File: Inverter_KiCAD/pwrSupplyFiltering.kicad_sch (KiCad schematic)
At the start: 10 parts

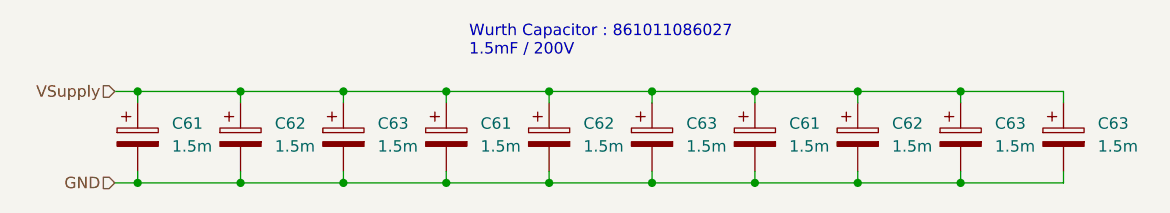
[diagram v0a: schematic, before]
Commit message: clear schematic errors
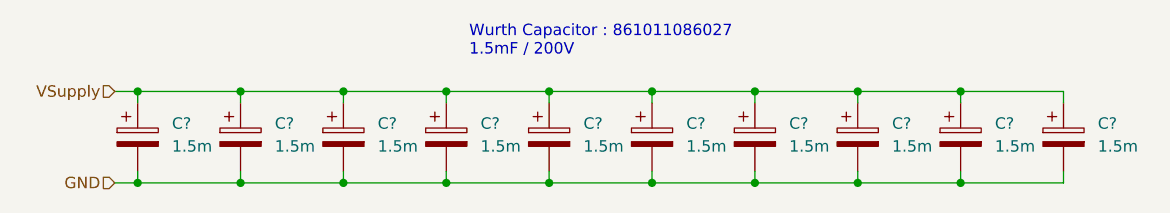
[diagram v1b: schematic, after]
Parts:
- renumbered C63 to C?, C61 to C?, C62 to C?
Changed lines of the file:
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@@
   (symbol (lib_id "Device:C_Polarized") (at 90.17 63.5 0) (unit 1)
     (in_bom yes) (on_board yes) (dnp no) (fields_autoplaced)
-    (property "Reference" "C63" (at 93.98 61.976 0)
+    (property "Reference" "C?" (at 93.98 61.976 0)
       (effects (font (size 1.27 1.27)) (justify left))
     )
@@
       (project "Inverter_KiCAD"
         (path "/5e6c1e3f-0815-454a-8acb-8e3e2d064875"
-          (reference "C63") (unit 1)
-        )
-        (path "/5e6c1e3f-0815-454a-8acb-8e3e2d064875/3abd505c-2b96-4cc2-9359-42e0642ca937"
-          (reference "C65") (unit 1)
+          (reference "C?") (unit 1)
+        )
+        (path "/5e6c1e3f-0815-454a-8acb-8e3e2d064875/3abd505c-2b96-4cc2-9359-42e0642ca937"
+          (reference "C1003") (unit 1)
         )
       )
@@
   (symbol (lib_id "Device:C_Polarized") (at 135.89 63.5 0) (unit 1)
     (in_bom yes) (on_board yes) (dnp no)
-    (property "Reference" "C61" (at 139.7 61.976 0)
+    (property "Reference" "C?" (at 139.7 61.976 0)
       (effects (font (size 1.27 1.27)) (justify left))
     )
@@
       (project "Inverter_KiCAD"
         (path "/5e6c1e3f-0815-454a-8acb-8e3e2d064875"
-          (reference "C61") (unit 1)
-        )
-        (path "/5e6c1e3f-0815-454a-8acb-8e3e2d064875/3abd505c-2b96-4cc2-9359-42e0642ca937"
-          (reference "C67") (unit 1)
+          (reference "C?") (unit 1)
+        )
+        (path "/5e6c1e3f-0815-454a-8acb-8e3e2d064875/3abd505c-2b96-4cc2-9359-42e0642ca937"
+          (reference "C1007") (unit 1)
         )
       )
@@
   (symbol (lib_id "Device:C_Polarized") (at 170.18 63.5 0) (unit 1)
     (in_bom yes) (on_board yes) (dnp no) (fields_autoplaced)
-    (property "Reference" "C63" (at 173.99 61.976 0)
+    (property "Reference" "C?" (at 173.99 61.976 0)
       (effects (font (size 1.27 1.27)) (justify left))
     )
@@
       (project "Inverter_KiCAD"
         (path "/5e6c1e3f-0815-454a-8acb-8e3e2d064875"
-          (reference "C63") (unit 1)
-        )
-        (path "/5e6c1e3f-0815-454a-8acb-8e3e2d064875/3abd505c-2b96-4cc2-9359-42e0642ca937"
-          (reference "C70") (unit 1)
+          (reference "C?") (unit 1)
+        )
+        (path "/5e6c1e3f-0815-454a-8acb-8e3e2d064875/3abd505c-2b96-4cc2-9359-42e0642ca937"
+          (reference "C1010") (unit 1)
         )
       )
@@
   (symbol (lib_id "Device:C_Polarized") (at 67.31 63.5 0) (unit 1)
     (in_bom yes) (on_board yes) (dnp no)
-    (property "Reference" "C61" (at 71.12 61.976 0)
+    (property "Reference" "C?" (at 71.12 61.976 0)
       (effects (font (size 1.27 1.27)) (justify left))
     )
@@
       (project "Inverter_KiCAD"
         (path "/5e6c1e3f-0815-454a-8acb-8e3e2d064875"
-          (reference "C61") (unit 1)
-        )
-        (path "/5e6c1e3f-0815-454a-8acb-8e3e2d064875/3abd505c-2b96-4cc2-9359-42e0642ca937"
-          (reference "C61") (unit 1)
+          (reference "C?") (unit 1)
+        )
+        (path "/5e6c1e3f-0815-454a-8acb-8e3e2d064875/3abd505c-2b96-4cc2-9359-42e0642ca937"
+          (reference "C1001") (unit 1)
         )
       )
@@
   (symbol (lib_id "Device:C_Polarized") (at 78.74 63.5 0) (unit 1)
     (in_bom yes) (on_board yes) (dnp no) (fields_autoplaced)
-    (property "Reference" "C62" (at 82.55 61.976 0)
+    (property "Reference" "C?" (at 82.55 61.976 0)
       (effects (font (size 1.27 1.27)) (justify left))
     )
@@
       (project "Inverter_KiCAD"
         (path "/5e6c1e3f-0815-454a-8acb-8e3e2d064875"
-          (reference "C62") (unit 1)
-        )
-        (path "/5e6c1e3f-0815-454a-8acb-8e3e2d064875/3abd505c-2b96-4cc2-9359-42e0642ca937"
-          (reference "C63") (unit 1)
+          (reference "C?") (unit 1)
+        )
+        (path "/5e6c1e3f-0815-454a-8acb-8e3e2d064875/3abd505c-2b96-4cc2-9359-42e0642ca937"
+          (reference "C1002") (unit 1)
         )
       )
@@
   (symbol (lib_id "Device:C_Polarized") (at 101.6 63.5 0) (unit 1)
     (in_bom yes) (on_board yes) (dnp no)
-    (property "Reference" "C61" (at 105.41 61.976 0)
+    (property "Reference" "C?" (at 105.41 61.976 0)
       (effects (font (size 1.27 1.27)) (justify left))
     )
@@
       (project "Inverter_KiCAD"
         (path "/5e6c1e3f-0815-454a-8acb-8e3e2d064875"
-          (reference "C61") (unit 1)
-        )
-        (path "/5e6c1e3f-0815-454a-8acb-8e3e2d064875/3abd505c-2b96-4cc2-9359-42e0642ca937"
-          (reference "C62") (unit 1)
+          (reference "C?") (unit 1)
+        )
+        (path "/5e6c1e3f-0815-454a-8acb-8e3e2d064875/3abd505c-2b96-4cc2-9359-42e0642ca937"
+          (reference "C1004") (unit 1)
         )
       )
@@
   (symbol (lib_id "Device:C_Polarized") (at 147.32 63.5 0) (unit 1)
     (in_bom yes) (on_board yes) (dnp no) (fields_autoplaced)
-    (property "Reference" "C62" (at 151.13 61.976 0)
+    (property "Reference" "C?" (at 151.13 61.976 0)
       (effects (font (size 1.27 1.27)) (justify left))
     )
@@
       (project "Inverter_KiCAD"
         (path "/5e6c1e3f-0815-454a-8acb-8e3e2d064875"
-          (reference "C62") (unit 1)
-        )
-        (path "/5e6c1e3f-0815-454a-8acb-8e3e2d064875/3abd505c-2b96-4cc2-9359-42e0642ca937"
-          (reference "C68") (unit 1)
+          (reference "C?") (unit 1)
+        )
+        (path "/5e6c1e3f-0815-454a-8acb-8e3e2d064875/3abd505c-2b96-4cc2-9359-42e0642ca937"
+          (reference "C1008") (unit 1)
         )
       )
@@
   (symbol (lib_id "Device:C_Polarized") (at 158.75 63.5 0) (unit 1)
     (in_bom yes) (on_board yes) (dnp no) (fields_autoplaced)
-    (property "Reference" "C63" (at 162.56 61.976 0)
+    (property "Reference" "C?" (at 162.56 61.976 0)
       (effects (font (size 1.27 1.27)) (justify left))
     )
@@
       (project "Inverter_KiCAD"
         (path "/5e6c1e3f-0815-454a-8acb-8e3e2d064875"
-          (reference "C63") (unit 1)
-        )
-        (path "/5e6c1e3f-0815-454a-8acb-8e3e2d064875/3abd505c-2b96-4cc2-9359-42e0642ca937"
-          (reference "C69") (unit 1)
+          (reference "C?") (unit 1)
+        )
+        (path "/5e6c1e3f-0815-454a-8acb-8e3e2d064875/3abd505c-2b96-4cc2-9359-42e0642ca937"
+          (reference "C1009") (unit 1)
         )
       )
@@
   (symbol (lib_id "Device:C_Polarized") (at 124.46 63.5 0) (unit 1)
     (in_bom yes) (on_board yes) (dnp no) (fields_autoplaced)
-    (property "Reference" "C63" (at 128.27 61.976 0)
+    (property "Reference" "C?" (at 128.27 61.976 0)
       (effects (font (size 1.27 1.27)) (justify left))
     )
@@
       (project "Inverter_KiCAD"
         (path "/5e6c1e3f-0815-454a-8acb-8e3e2d064875"
-          (reference "C63") (unit 1)
-        )
-        (path "/5e6c1e3f-0815-454a-8acb-8e3e2d064875/3abd505c-2b96-4cc2-9359-42e0642ca937"
-          (reference "C66") (unit 1)
+          (reference "C?") (unit 1)
+        )
+        (path "/5e6c1e3f-0815-454a-8acb-8e3e2d064875/3abd505c-2b96-4cc2-9359-42e0642ca937"
+          (reference "C1006") (unit 1)
         )
       )
@@
   (symbol (lib_id "Device:C_Polarized") (at 113.03 63.5 0) (unit 1)
     (in_bom yes) (on_board yes) (dnp no) (fields_autoplaced)
-    (property "Reference" "C62" (at 116.84 61.976 0)
+    (property "Reference" "C?" (at 116.84 61.976 0)
       (effects (font (size 1.27 1.27)) (justify left))
     )
@@
       (project "Inverter_KiCAD"
         (path "/5e6c1e3f-0815-454a-8acb-8e3e2d064875"
-          (reference "C62") (unit 1)
-        )
-        (path "/5e6c1e3f-0815-454a-8acb-8e3e2d064875/3abd505c-2b96-4cc2-9359-42e0642ca937"
-          (reference "C64") (unit 1)
-        )
-      )
+          (reference "C?") (unit 1)
+        )
+        (path "/5e6c1e3f-0815-454a-8acb-8e3e2d064875/3abd505c-2b96-4cc2-9359-42e0642ca937"
+          (reference "C1005") (unit 1)
+        )
+      )

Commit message: end of sch, start pcb
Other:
- company: (none) -> ENSEA
- title: (none) -> AAP Inverter
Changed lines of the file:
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@@
 (kicad_sch (version 20230121) (generator eeschema)
   (paper "A4")
+  (title_block
+    (title "AAP Inverter")
+    (date "2023-05-01")
+    (company "ENSEA")
+  )
   (junction (at 90.17 58.42) (diameter 0) (color 0 0 0 0)
   )

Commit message: rooting done
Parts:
- removed C?: 1.5m, Capacitor_THT:CP_Radial_D35.0mm_P10.00mm_SnapIn, symbol Device:C_Polarized

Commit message: change pcb
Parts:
- removed C? (x4): 1.5m, Capacitor_THT:CP_Radial_D35.0mm_P10.00mm_SnapIn, symbol Device:C_Polarized
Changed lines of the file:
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@@
     (company "ENSEA")
   )
-  (junction (at 90.17 58.42) (diameter 0) (color 0 0 0 0)
-  )
-  (junction (at 113.03 58.42) (diameter 0) (color 0 0 0 0)
-  )
   (junction (at 147.32 68.58) (diameter 0) (color 0 0 0 0)
   )
-  (junction (at 78.74 68.58) (diameter 0) (color 0 0 0 0)
-  )
-  (junction (at 101.6 58.42) (diameter 0) (color 0 0 0 0)
-  )
   (junction (at 124.46 58.42) (diameter 0) (color 0 0 0 0)
   )
@@
   (junction (at 147.32 58.42) (diameter 0) (color 0 0 0 0)
   )
-  (junction (at 113.03 68.58) (diameter 0) (color 0 0 0 0)
-  )
-  (junction (at 90.17 68.58) (diameter 0) (color 0 0 0 0)
-  )
-  (junction (at 101.6 68.58) (diameter 0) (color 0 0 0 0)
-  )
-  (junction (at 78.74 58.42) (diameter 0) (color 0 0 0 0)
-  )
   (junction (at 124.46 68.58) (diameter 0) (color 0 0 0 0)
   )
@@
     (stroke (width 0) (type default))
   )
-  (wire (pts (xy 113.03 68.58) (xy 124.46 68.58))
-    (stroke (width 0) (type default))
-  )
-  (wire (pts (xy 90.17 58.42) (xy 101.6 58.42))
-    (stroke (width 0) (type default))
-  )
-  (wire (pts (xy 90.17 68.58) (xy 101.6 68.58))
-    (stroke (width 0) (type default))
-  )
-  (wire (pts (xy 101.6 68.58) (xy 113.03 68.58))
+  (wire (pts (xy 109.22 68.58) (xy 124.46 68.58))
     (stroke (width 0) (type default))
   )
@@
     (stroke (width 0) (type default))
   )
-  (wire (pts (xy 113.03 58.42) (xy 124.46 58.42))
+  (wire (pts (xy 109.22 58.42) (xy 124.46 58.42))
     (stroke (width 0) (type default))
   )
@@
     (stroke (width 0) (type default))
   )
-  (wire (pts (xy 90.17 58.42) (xy 90.17 59.69))
-    (stroke (width 0) (type default))
-  )
-  (wire (pts (xy 101.6 58.42) (xy 113.03 58.42))
-    (stroke (width 0) (type default))
-  )
   (wire (pts (xy 135.89 67.31) (xy 135.89 68.58))
     (stroke (width 0) (type default))
@@
     (stroke (width 0) (type default))
   )
-  (wire (pts (xy 113.03 67.31) (xy 113.03 68.58))
-    (stroke (width 0) (type default))
-  )
-  (wire (pts (xy 90.17 67.31) (xy 90.17 68.58))
-    (stroke (width 0) (type default))
-  )
-  (wire (pts (xy 74.93 58.42) (xy 78.74 58.42))
-    (stroke (width 0) (type default))
-  )
-  (wire (pts (xy 78.74 58.42) (xy 90.17 58.42))
-    (stroke (width 0) (type default))
-  )
   (wire (pts (xy 170.18 59.69) (xy 170.18 58.42))
     (stroke (width 0) (type default))
   )
-  (wire (pts (xy 101.6 67.31) (xy 101.6 68.58))
-    (stroke (width 0) (type default))
-  )
-  (wire (pts (xy 78.74 68.58) (xy 90.17 68.58))
-    (stroke (width 0) (type default))
-  )
   (wire (pts (xy 124.46 68.58) (xy 135.89 68.58))
     (stroke (width 0) (type default))
@@
     (stroke (width 0) (type default))
   )
-  (wire (pts (xy 113.03 58.42) (xy 113.03 59.69))
-    (stroke (width 0) (type default))
-  )
-  (wire (pts (xy 74.93 68.58) (xy 78.74 68.58))
-    (stroke (width 0) (type default))
-  )
-  (wire (pts (xy 78.74 58.42) (xy 78.74 59.69))
-    (stroke (width 0) (type default))
-  )
   (wire (pts (xy 147.32 67.31) (xy 147.32 68.58))
     (stroke (width 0) (type default))
@@
   )
   (wire (pts (xy 158.75 68.58) (xy 170.18 68.58))
-    (stroke (width 0) (type default))
-  )
-  (wire (pts (xy 78.74 67.31) (xy 78.74 68.58))
-    (stroke (width 0) (type default))
-  )
-  (wire (pts (xy 101.6 59.69) (xy 101.6 58.42))
     (stroke (width 0) (type default))
   )
@@
     (effects (font (size 1.27 1.27)) (justify left bottom))
   )
-  (hierarchical_label "VSupply" (shape input) (at 74.93 58.42 180) (fields_autoplaced)
+  (hierarchical_label "VSupply" (shape input) (at 109.22 58.42 180) (fields_autoplaced)
     (effects (font (size 1.27 1.27)) (justify right))
   )
-  (hierarchical_label "GND" (shape input) (at 74.93 68.58 180) (fields_autoplaced)
+  (hierarchical_label "GND" (shape input) (at 109.22 68.58 180) (fields_autoplaced)
     (effects (font (size 1.27 1.27)) (justify right))
-  )
-  (symbol (lib_id "Device:C_Polarized") (at 90.17 63.5 0) (unit 1)
-    (in_bom yes) (on_board yes) (dnp no) (fields_autoplaced)
-    (property "Reference" "C?" (at 93.98 61.976 0)
-      (effects (font (size 1.27 1.27)) (justify left))
-    )
-    (property "Value" "1.5m" (at 93.98 64.516 0)
-      (effects (font (size 1.27 1.27)) (justify left))
-    )
-    (property "Footprint" "Capacitor_THT:CP_Radial_D35.0mm_P10.00mm_SnapIn" (at 91.1352 67.31 0)
-      (effects (font (size 1.27 1.27)) hide)
-    )
-    (property "Datasheet" "~" (at 90.17 63.5 0)
-      (effects (font (size 1.27 1.27)) hide)
-    )
-    (pin "1")
-    (pin "2")
-    (instances
-      (project "Inverter_KiCAD"
-        (path "/5e6c1e3f-0815-454a-8acb-8e3e2d064875"
-          (reference "C?") (unit 1)
-        )
-        (path "/5e6c1e3f-0815-454a-8acb-8e3e2d064875/3abd505c-2b96-4cc2-9359-42e0642ca937"
-          (reference "C1002") (unit 1)
-        )
-      )
-    )
   )
   (symbol (lib_id "Device:C_Polarized") (at 135.89 63.5 0) (unit 1)
@@
     )
   )
-  (symbol (lib_id "Device:C_Polarized") (at 78.74 63.5 0) (unit 1)
-    (in_bom yes) (on_board yes) (dnp no) (fields_autoplaced)
-    (property "Reference" "C?" (at 82.55 61.976 0)
-      (effects (font (size 1.27 1.27)) (justify left))
-    )
-    (property "Value" "1.5m" (at 82.55 64.516 0)
-      (effects (font (size 1.27 1.27)) (justify left))
-    )
-    (property "Footprint" "Capacitor_THT:CP_Radial_D35.0mm_P10.00mm_SnapIn" (at 79.7052 67.31 0)
-      (effects (font (size 1.27 1.27)) hide)
-    )
-    (property "Datasheet" "~" (at 78.74 63.5 0)
-      (effects (font (size 1.27 1.27)) hide)
-    )
-    (pin "1")
-    (pin "2")
-    (instances
-      (project "Inverter_KiCAD"
-        (path "/5e6c1e3f-0815-454a-8acb-8e3e2d064875"
-          (reference "C?") (unit 1)
-        )
-        (path "/5e6c1e3f-0815-454a-8acb-8e3e2d064875/3abd505c-2b96-4cc2-9359-42e0642ca937"
-          (reference "C1001") (unit 1)
-        )
-      )
-    )
-  )
-  (symbol (lib_id "Device:C_Polarized") (at 101.6 63.5 0) (unit 1)
-    (in_bom yes) (on_board yes) (dnp no)
-    (property "Reference" "C?" (at 105.41 61.976 0)
-      (effects (font (size 1.27 1.27)) (justify left))
-    )
-    (property "Value" "1.5m" (at 105.41 64.516 0)
-      (effects (font (size 1.27 1.27)) (justify left))
-    )
-    (property "Footprint" "Capacitor_THT:CP_Radial_D35.0mm_P10.00mm_SnapIn" (at 102.5652 67.31 0)
-      (effects (font (size 1.27 1.27)) hide)
-    )
-    (property "Datasheet" "~" (at 101.6 63.5 0)
-      (effects (font (size 1.27 1.27)) hide)
-    )
-    (pin "1")
-    (pin "2")
-    (instances
-      (project "Inverter_KiCAD"
-        (path "/5e6c1e3f-0815-454a-8acb-8e3e2d064875"
-          (reference "C?") (unit 1)
-        )
-        (path "/5e6c1e3f-0815-454a-8acb-8e3e2d064875/3abd505c-2b96-4cc2-9359-42e0642ca937"
-          (reference "C1003") (unit 1)
-        )
-      )
-    )
-  )
   (symbol (lib_id "Device:C_Polarized") (at 147.32 63.5 0) (unit 1)
     (in_bom yes) (on_board yes) (dnp no) (fields_autoplaced)
@@
         )
       )
-    )
-  )
-  (symbol (lib_id "Device:C_Polarized") (at 113.03 63.5 0) (unit 1)
-    (in_bom yes) (on_board yes) (dnp no) (fields_autoplaced)
-    (property "Reference" "C?" (at 116.84 61.976 0)
-      (effects (font (size 1.27 1.27)) (justify left))
-    )
-    (property "Value" "1.5m" (at 116.84 64.516 0)
-      (effects (font (size 1.27 1.27)) (justify left))
-    )
-    (property "Footprint" "Capacitor_THT:CP_Radial_D35.0mm_P10.00mm_SnapIn" (at 113.9952 67.31 0)
-      (effects (font (size 1.27 1.27)) hide)
-    )
-    (property "Datasheet" "~" (at 113.03 63.5 0)
-      (effects (font (size 1.27 1.27)) hide)
-    )
-    (pin "1")
-    (pin "2")
-    (instances
-      (project "Inverter_KiCAD"
-        (path "/5e6c1e3f-0815-454a-8acb-8e3e2d064875"
-          (reference "C?") (unit 1)
-        )
-        (path "/5e6c1e3f-0815-454a-8acb-8e3e2d064875/3abd505c-2b96-4cc2-9359-42e0642ca937"
-          (reference "C1004") (unit 1)
-        )
-      )

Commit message: update pcb
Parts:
- C? (x5): Fournisseur (none) -> Wurth; MFR (none) -> 861 011 086 027
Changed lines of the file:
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@@
+      (effects (font (size 1.27 1.27)) hide)
+    )
+    (property "Fournisseur" "Wurth" (at 135.89 63.5 0)
+      (effects (font (size 1.27 1.27)) hide)
+    )
+    (property "MFR" "861 011 086 027" (at 135.89 63.5 0)
       (effects (font (size 1.27 1.27)) hide)
     )
@@
         )
         (path "/5e6c1e3f-0815-454a-8acb-8e3e2d064875/3abd505c-2b96-4cc2-9359-42e0642ca937"
-          (reference "C1006") (unit 1)
+          (reference "C1002") (unit 1)
         )
       )
@@
       (effects (font (size 1.27 1.27)) hide)
     )
+    (property "Fournisseur" "Wurth" (at 170.18 63.5 0)
+      (effects (font (size 1.27 1.27)) hide)
+    )
+    (property "MFR" "861 011 086 027" (at 170.18 63.5 0)
+      (effects (font (size 1.27 1.27)) hide)
+    )
     (pin "1")
     (pin "2")
@@
         )
         (path "/5e6c1e3f-0815-454a-8acb-8e3e2d064875/3abd505c-2b96-4cc2-9359-42e0642ca937"
-          (reference "C1009") (unit 1)
+          (reference "C1005") (unit 1)
         )
       )
@@
       (effects (font (size 1.27 1.27)) hide)
     )
+    (property "Fournisseur" "Wurth" (at 147.32 63.5 0)
+      (effects (font (size 1.27 1.27)) hide)
+    )
+    (property "MFR" "861 011 086 027" (at 147.32 63.5 0)
+      (effects (font (size 1.27 1.27)) hide)
+    )
     (pin "1")
     (pin "2")
@@
         )
         (path "/5e6c1e3f-0815-454a-8acb-8e3e2d064875/3abd505c-2b96-4cc2-9359-42e0642ca937"
-          (reference "C1007") (unit 1)
+          (reference "C1003") (unit 1)
         )
       )
@@
       (effects (font (size 1.27 1.27)) hide)
     )
+    (property "Fournisseur" "Wurth" (at 158.75 63.5 0)
+      (effects (font (size 1.27 1.27)) hide)
+    )
+    (property "MFR" "861 011 086 027" (at 158.75 63.5 0)
+      (effects (font (size 1.27 1.27)) hide)
+    )
     (pin "1")
     (pin "2")
@@
         )
         (path "/5e6c1e3f-0815-454a-8acb-8e3e2d064875/3abd505c-2b96-4cc2-9359-42e0642ca937"
-          (reference "C1008") (unit 1)
+          (reference "C1004") (unit 1)
         )
       )
@@
       (effects (font (size 1.27 1.27)) hide)
     )
+    (property "Fournisseur" "Wurth" (at 124.46 63.5 0)
+      (effects (font (size 1.27 1.27)) hide)
+    )
+    (property "MFR" "861 011 086 027" (at 124.46 63.5 0)
+      (effects (font (size 1.27 1.27)) hide)
+    )
     (pin "1")
     (pin "2")
@@
         )
         (path "/5e6c1e3f-0815-454a-8acb-8e3e2d064875/3abd505c-2b96-4cc2-9359-42e0642ca937"
-          (reference "C1005") (unit 1)
+          (reference "C1001") (unit 1)
         )
       )
